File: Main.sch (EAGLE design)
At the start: 34 parts, among them IC2 74AHC1G125DBV, IC3 74AHC1G125DBV, M1 HX1, X1 BU-SMA-V

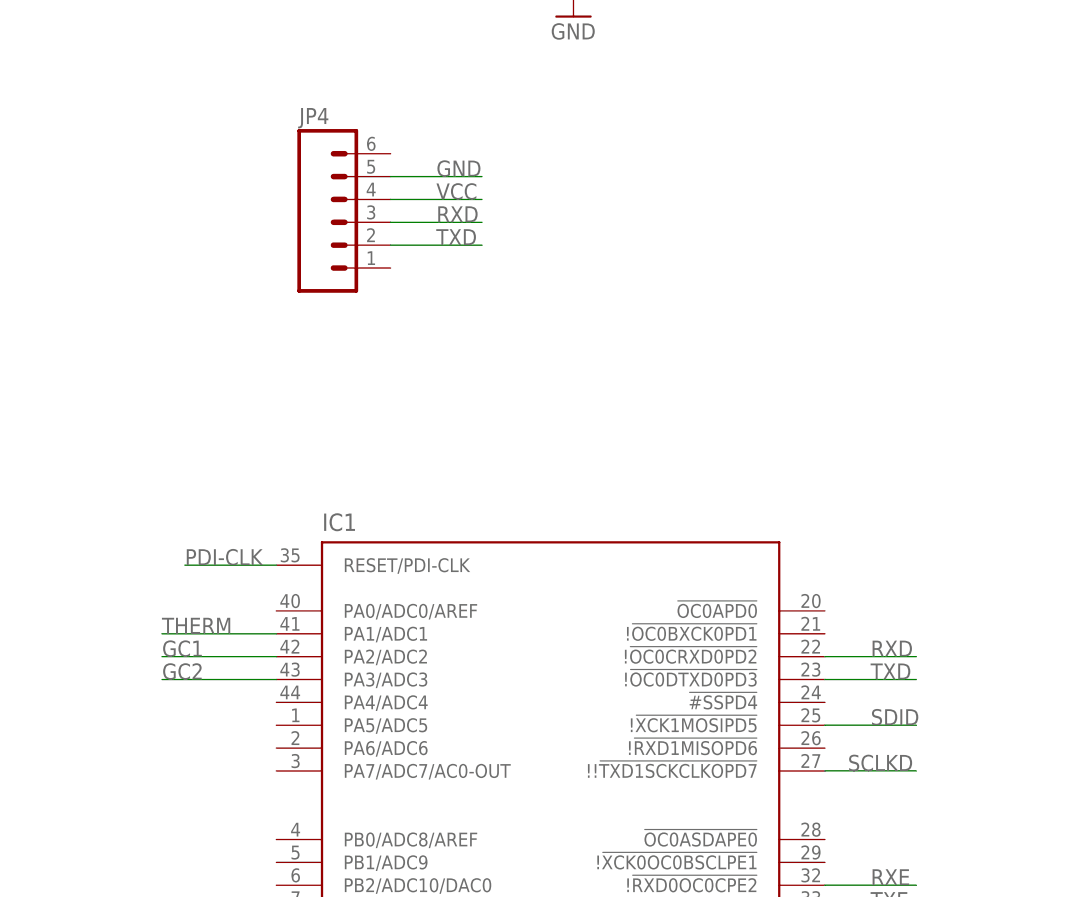
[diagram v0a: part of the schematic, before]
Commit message: Add LED for nerde programmers
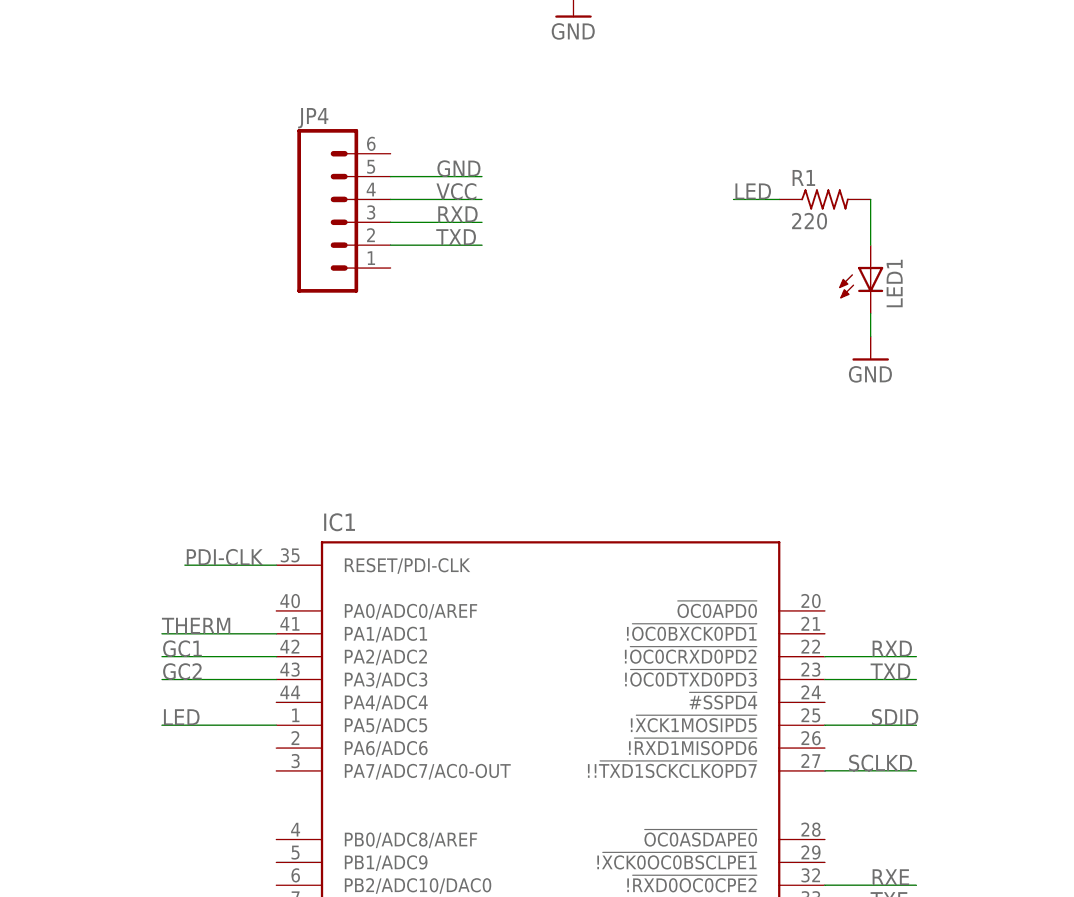
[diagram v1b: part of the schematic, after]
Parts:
- added LED1: (no value), led:LEDCHIP-LED0603
- added R1: 220, rcl:R-US_R0603
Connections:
- new net LED: IC1.PA5/ADC5, R1.1
- new net N$11: LED1.A, R1.2
- net GND: now also LED1.C
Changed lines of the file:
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@@
 <?xml version="1.0" encoding="utf-8"?>
 <!DOCTYPE eagle SYSTEM "eagle.dtd">
-<eagle version="8.1.0">
+<eagle version="6.5.0">
 <drawing>
 <settings>
@@
 <part name="U$12" library="SHC" deviceset="CKN10160-ND" device=""/>
 <part name="GND13" library="SparkFun" deviceset="GND" device=""/>
+<part name="LED1" library="led" deviceset="LED" device="CHIP-LED0603"/>
+<part name="R1" library="rcl" deviceset="R-US_" device="R0603" value="220"/>
+<part name="GND16" library="SparkFun-Aesthetics" deviceset="GND" device=""/>
 </parts>
 <sheets>
@@
 <instance part="U$12" gate="G$1" x="-23.368" y="-30.48" rot="MR0"/>
 <instance part="GND13" gate="1" x="-7.62" y="180.34"/>
+<instance part="LED1" gate="G$1" x="114.3" y="139.7"/>
+<instance part="R1" gate="G$1" x="109.22" y="147.32"/>
+<instance part="GND16" gate="1" x="114.3" y="129.54"/>
 </instances>
 <busses>
@@
 <junction x="-7.62" y="190.5"/>
 <pinref part="GND13" gate="1" pin="GND"/>
+</segment>
+<segment>
+<pinref part="LED1" gate="G$1" pin="C"/>
+<wire x1="114.3" y1="134.62" x2="114.3" y2="132.08" width="0.1524" layer="91"/>
+<pinref part="GND16" gate="1" pin="GND"/>
 </segment>
 </net>
@@
 </segment>
 </net>
+<net name="N$11" class="0">
+<segment>
+<pinref part="R1" gate="G$1" pin="2"/>
+<pinref part="LED1" gate="G$1" pin="A"/>
+<wire x1="114.3" y1="147.32" x2="114.3" y2="142.24" width="0.1524" layer="91"/>
+</segment>
+</net>
+<net name="LED" class="0">
+<segment>
+<pinref part="IC1" gate="G$1" pin="PA5/ADC5"/>
+<wire x1="48.26" y1="88.9" x2="35.56" y2="88.9" width="0.1524" layer="91"/>
+<label x="35.56" y="88.9" size="1.778" layer="95"/>
+</segment>
+<segment>
+<pinref part="R1" gate="G$1" pin="1"/>
+<wire x1="104.14" y1="147.32" x2="99.06" y2="147.32" width="0.1524" layer="91"/>
+<label x="99.06" y="147.32" size="1.778" layer="95"/>
+</segment>
+</net>
